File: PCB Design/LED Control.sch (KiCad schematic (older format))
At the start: 26 parts, among them J1 5V 5A Power, J2 TO WS2812B LED STRIP, J3 Sound Sensor, SW1 SW_Push_Dual

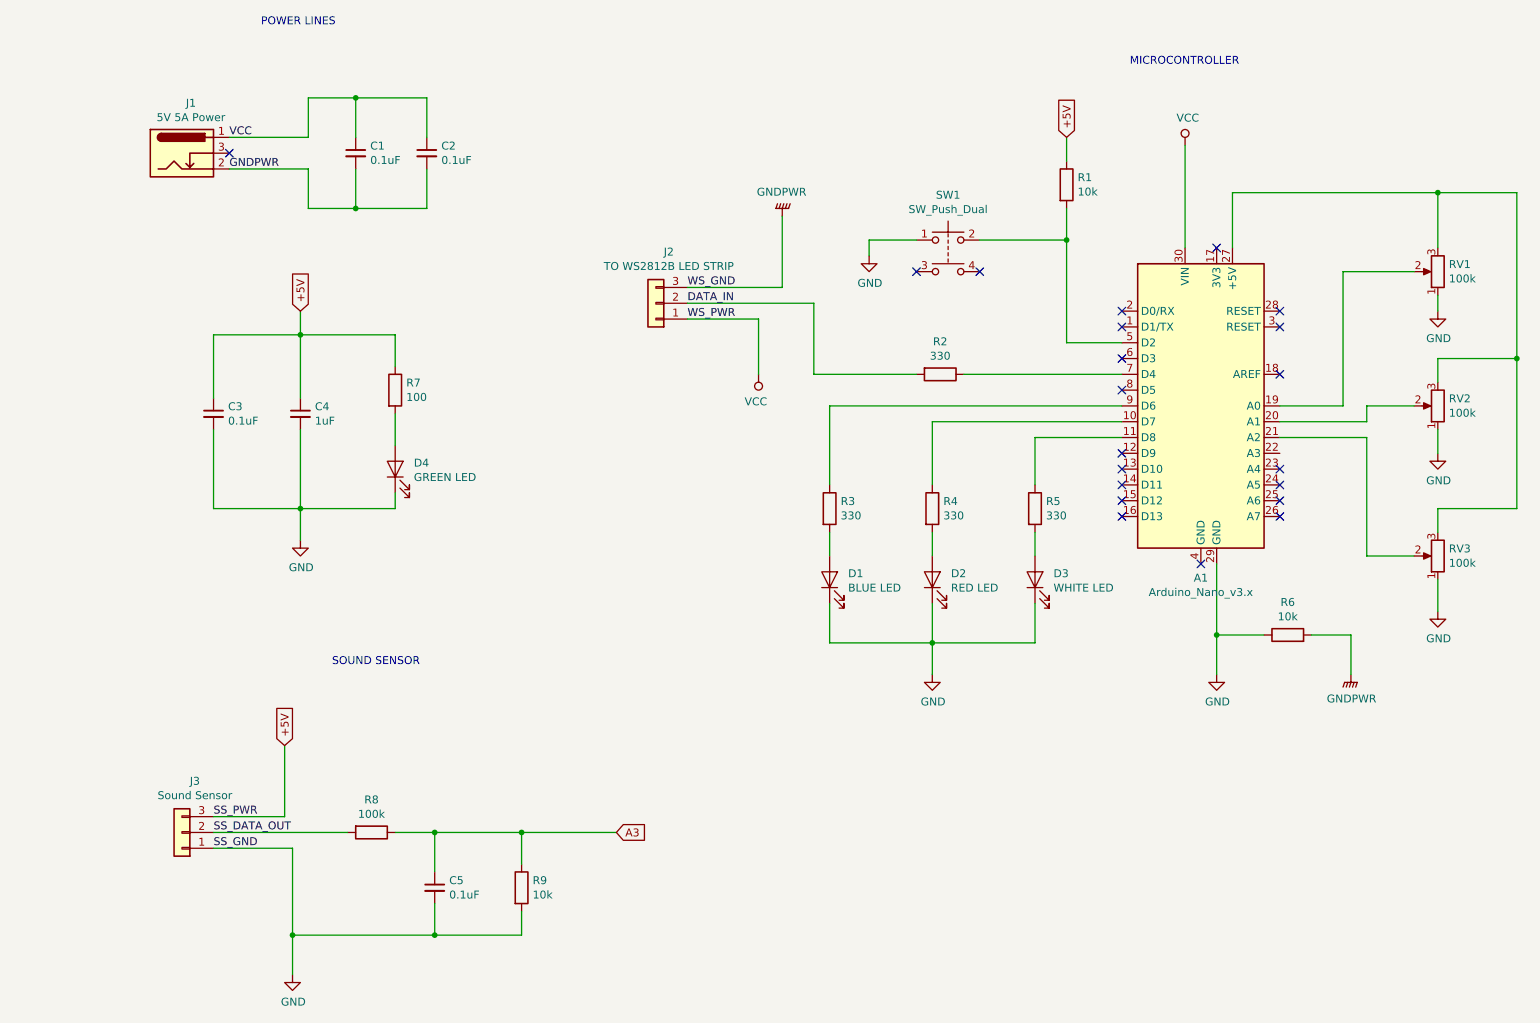
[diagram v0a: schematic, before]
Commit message: edge cuts and M3 mounting holes added
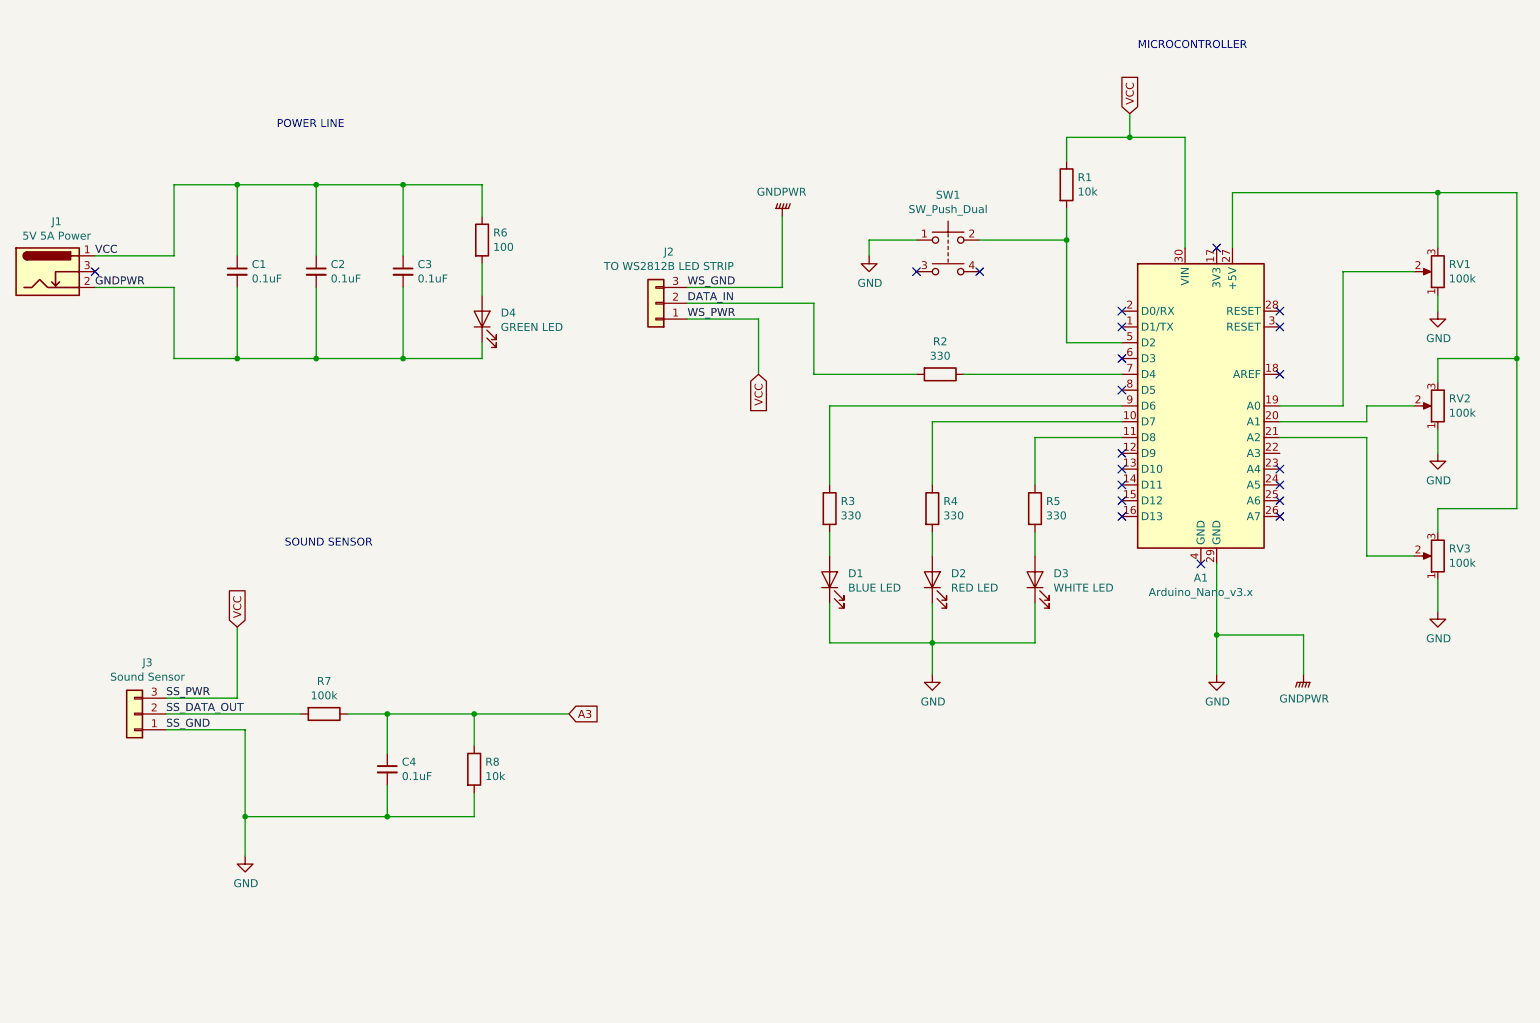
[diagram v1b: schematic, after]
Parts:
- removed C4: 1uF, Capacitor_SMD:C_0603_1608Metric, symbol Device:C_Small
- removed R6: 10k, Resistor_SMD:R_0805_2012Metric, symbol Device:R
- renumbered C5 to C4, R7 to R6, R8 to R7, R9 to R8
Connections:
- net +5V is gone; now on net VCC: C3.1, J3.3 (Pin_3), R1.1, R6.1
- net GNDPWR is gone; now on net GND: C1.2, C2.2, J1.2, J2.3 (Pin_3)
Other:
- note added: "POWER LINE"
- note removed: "POWER LINES"
- moved on the sheet: C1, C2, C3, C4, D4, J1, J3, R6, R7, R8

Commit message: power, gnd planes and traces
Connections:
- net A3: now also A1.22 (A3)
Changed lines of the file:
@@
 Wire Wire Line
 	8500 5000 9050 5000
+Text GLabel 8950 3850 2    50   Input ~ 0
+A3
+Wire Wire Line
+	8900 3850 8950 3850
 $EndSCHEMATC

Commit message: PCB completed
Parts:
- SW1: footprint Button_Switch_THT:SW_PUSH_6mm_H13mm -> Custom Footprint:Push_Button_Switch
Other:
- moved on the sheet: A1, C1, C2, C3, C4, D1, D2, D3, D4, J1, J2, J3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
